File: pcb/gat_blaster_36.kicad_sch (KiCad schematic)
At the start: 25 parts, among them J1 Conn_01x05_Pin, J2 USB_C_Receptacle_USB2.0, SW1 SW_Push, SW2 SW_Push, U1 STM32F072CBTx, U2 TLV1117-33, Y1 8MHz

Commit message: Added USB 5V filter
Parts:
- added C12: 10n, symbol Device:C
- added C13: 100n, symbol Device:C
- added C14: 4.7u, symbol Device:C
- added C15, C16: 10p, symbol Device:C
- added FB2: 120, symbol Device:FerriteBead
- added R6, R7: 10R, symbol Device:R
- FB1: value 120 -> 120R
- R3: value 0 -> 0R
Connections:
- net GND: now also C12.2, C13.2, C14.2, C15.2, C16.2
- net SWCLK: now also D1.3 (IO2); no longer D1.6 (IO5)
- net SWDIO: now also D1.4 (IO3); no longer D1.5 (IO4)
- net USB_D+: now also D1.5 (IO4), R6.2; no longer D1.4 (IO3), J2.A6 (D+), J2.B6 (D+)
- net USB_D-: now also D1.6 (IO5), R7.2; no longer D1.3 (IO2), J2.A7 (D-), J2.B7 (D-)
- net VBUS: now also C12.1, FB2.1; no longer C10.1, U2.3 (VI)
- new net: C15.1, J2.A6 (D+), J2.B6 (D+), R6.1
- new net: C16.1, J2.A7 (D-), J2.B7 (D-), R7.1
- new net +5V: C10.1, C13.1, C14.1, FB2.2, U2.3 (VI)
- no-connect marks 1 -> 3
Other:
- moved on the sheet: C1, C10, C11, C2, C3, C4, C5, C6, C7, C8, C9, D1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

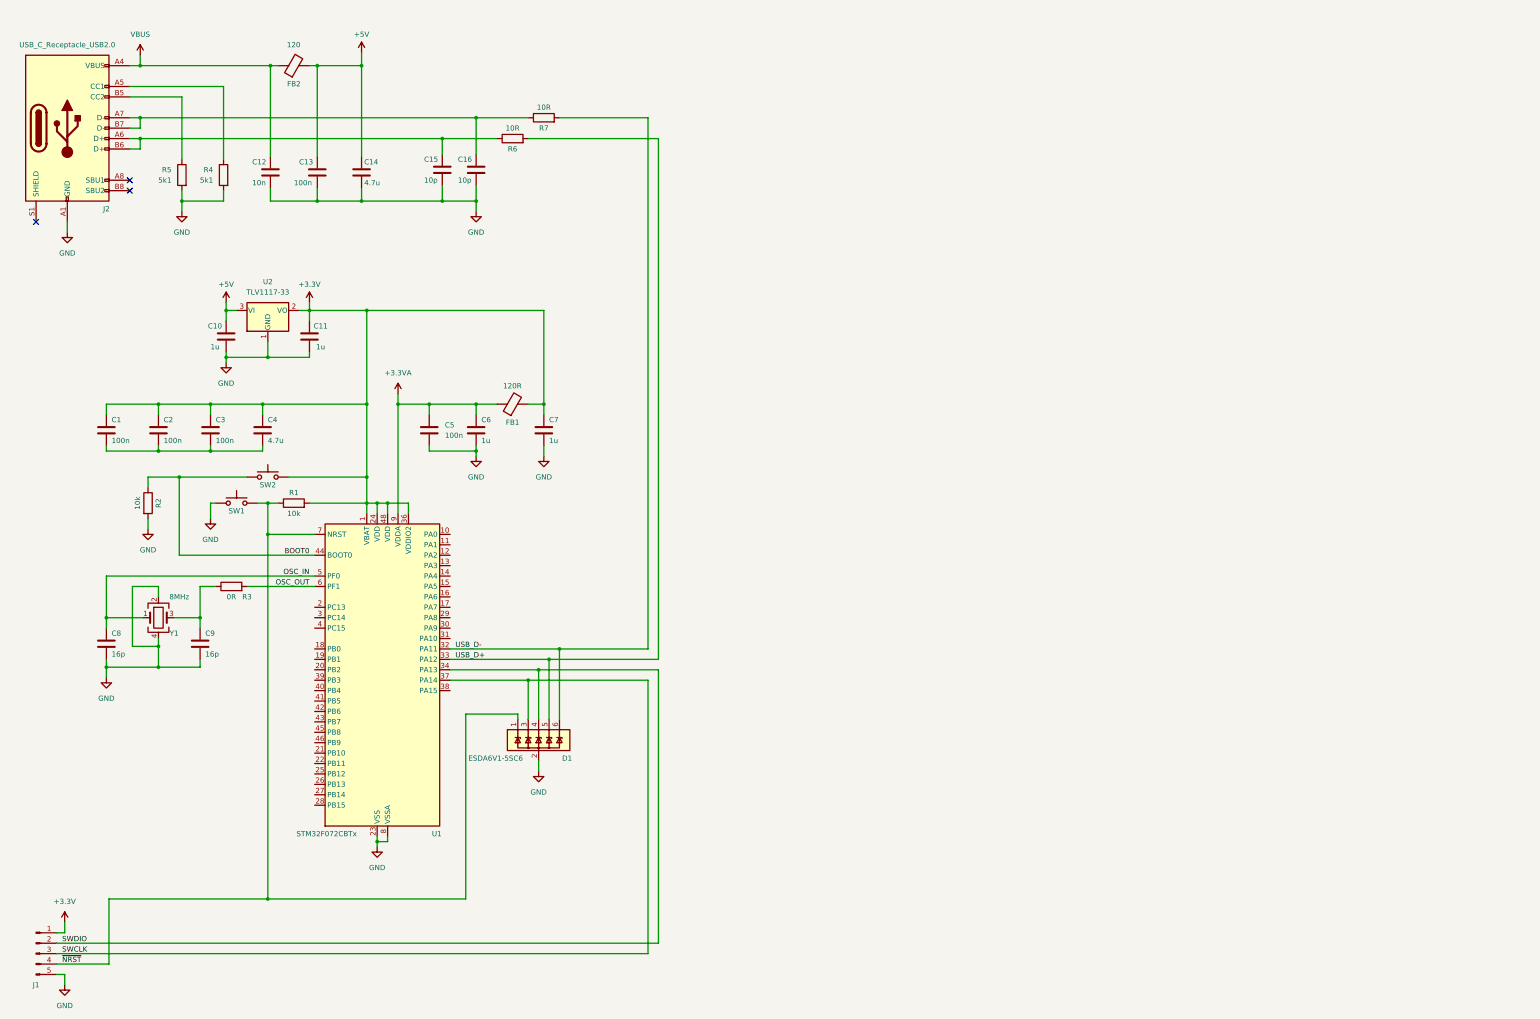
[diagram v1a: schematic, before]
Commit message: Added series resistors on data lines, changed left/right communication cable to HDMI connector, fully supported by single micro.
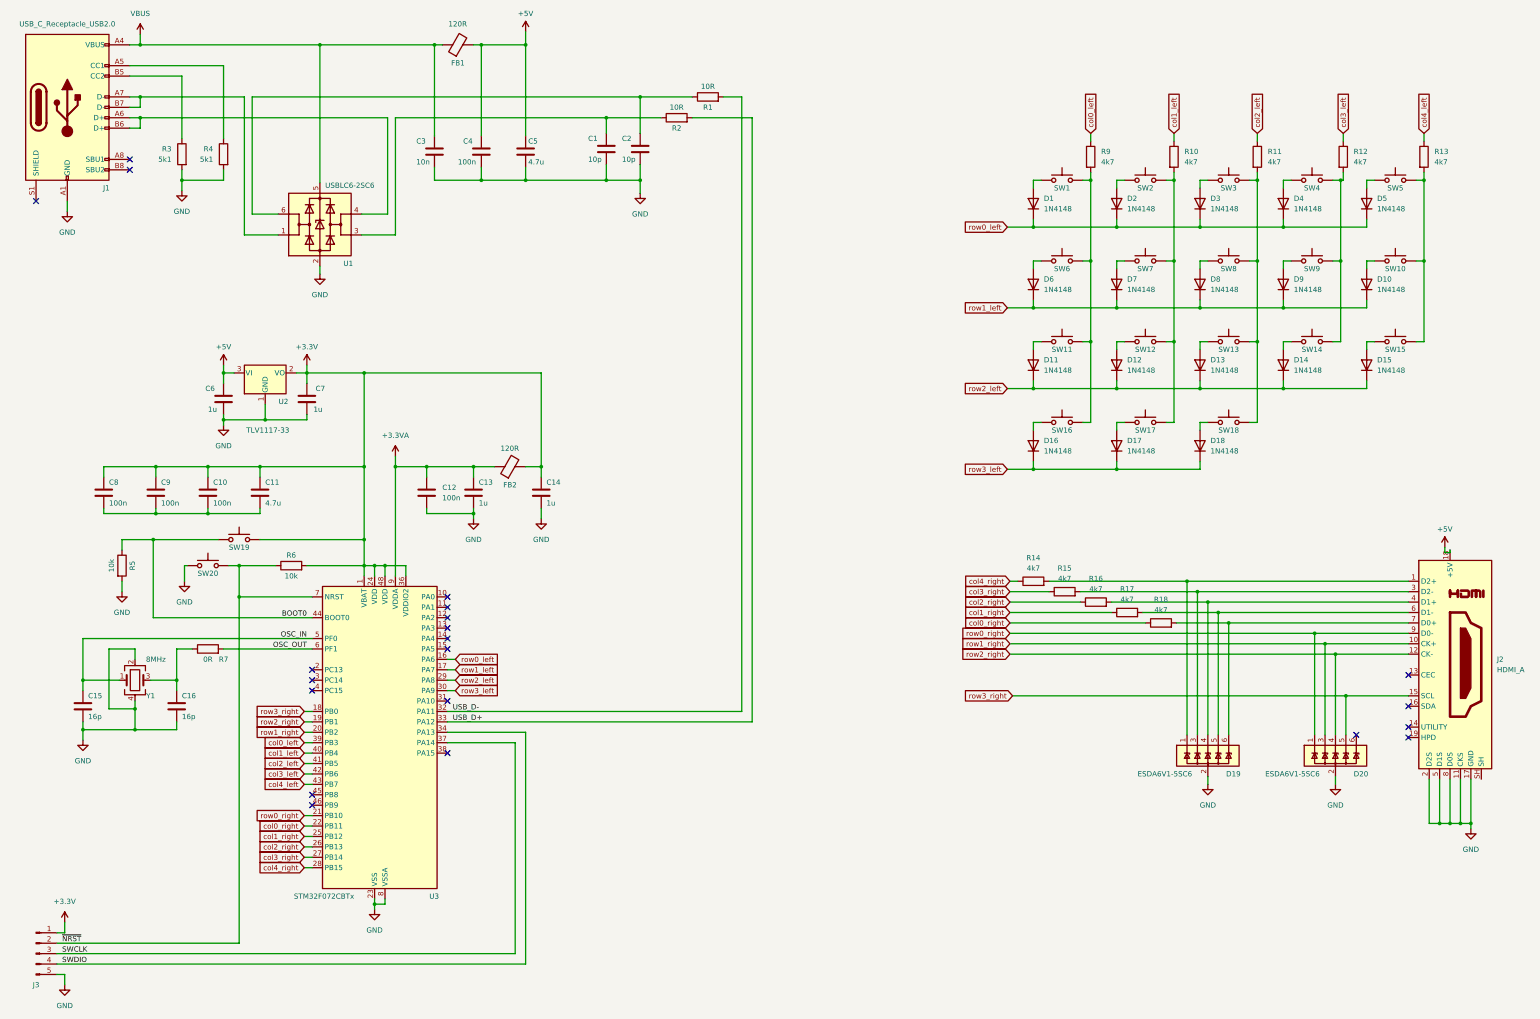
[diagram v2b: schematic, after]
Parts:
- removed D1: ESDA6V1-5SC6, Package_TO_SOT_SMD:SOT-23-6, symbol Power_Protection:ESDA6V1-5SC6
- added D1, D10, D11, D12, D13, D14, D15, D16, D17, D18, D2, D3, D4, D5, D6, D7, D8, D9: 1N4148, kbd:sod123_mmszxxxt1g, symbol Diode:1N4148
- added D19, D20: ESDA6V1-5SC6, kbd:sot23-6L_usblc6-2, symbol Power_Protection:ESDA6V1-5SC6
- added J2: HDMI_A, kbd:hdmi_cnc_tech_2000-1-1-20-00-bk, symbol Connector:HDMI_A
- added R10, R11, R12, R13, R14, R15, R16, R17, R18, R9: 4k7, kbd:0603, symbol Device:R
- added SW1, SW10, SW11, SW12, SW13, SW14, SW15, SW16, SW17, SW18, SW2, SW3, SW4, SW5, SW6, SW7, SW8, SW9: SW_Push, kbd:gateron_pro_5_reversible, symbol Switch:SW_Push
- added U1: USBLC6-2SC6, kbd:sot23-6L_usblc6-2, symbol Power_Protection:USBLC6-2SC6
- C1: renamed from C15; footprint (none) -> kbd:0603
- C10: renamed from C3; footprint (none) -> kbd:0603
- C11: renamed from C4; footprint (none) -> kbd:0603
- C12: renamed from C5; footprint (none) -> kbd:0603
- C13: renamed from C6; footprint (none) -> kbd:0603
- C14: renamed from C7; footprint (none) -> kbd:0603
- C15: renamed from C8; footprint (none) -> kbd:0603
- C16: renamed from C9; footprint (none) -> kbd:0603
- C2: renamed from C16; footprint (none) -> kbd:0603
- C3: renamed from C12; footprint (none) -> kbd:0603
- C4: renamed from C13; footprint (none) -> kbd:0603
- C5: renamed from C14; footprint (none) -> kbd:0603
- C6: renamed from C10; footprint (none) -> kbd:0603
- C7: renamed from C11; footprint (none) -> kbd:0603
- C8: renamed from C1; footprint (none) -> kbd:0603
- C9: renamed from C2; footprint (none) -> kbd:0603
- FB1: renamed from FB2; value 120 -> 120R; footprint (none) -> kbd:0603
- FB2: renamed from FB1; footprint (none) -> kbd:0603
- J1: renamed from J2; footprint (none) -> kbd:usb-c_usb4085
- J3: renamed from J1; footprint (none) -> kbd:SIP-5
- R1: renamed from R7; footprint (none) -> kbd:0603
- R2: renamed from R6; footprint (none) -> kbd:0603
- R3: renamed from R5; footprint (none) -> kbd:0603
- R4: footprint (none) -> kbd:0603
- R5: renamed from R2; footprint (none) -> kbd:0603
- R6: renamed from R1; footprint (none) -> kbd:0603
- R7: renamed from R3; footprint (none) -> kbd:0603
- SW19: renamed from SW2; footprint (none) -> kbd:sw_pts647
- SW20: renamed from SW1; footprint (none) -> kbd:sw_pts647
- U2: footprint (none) -> kbd:sot223_tl1117
- U3: renamed from U1; footprint Package_QFP:LQFP-48_7x7mm_P0.5mm -> kbd:QFP-48_7x7_Pitch0.5mm
- Y1: footprint (none) -> kbd:osc_ecx-32
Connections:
- net +5V: now also J2.18 (+5V)
- net GND: now also D19.2 (GND), D20.2 (GND), J2.11 (CKS), J2.17 (GND), J2.2 (D2S), J2.5 (D1S), J2.8 (D0S), U1.2 (GND)
- net SWDIO: now also J3.4 (Pin_4); no longer J3.2 (Pin_2)
- net VBUS: now also U1.5 (VBUS)
- net ~{NRST}: now also J3.2 (Pin_2); no longer J3.4 (Pin_4)
- net at C1.1, R2.1: now also U1.3 (I/O2); no longer J1.A6 (D+), J1.B6 (D+)
- net at C2.1, R1.1: now also U1.6 (I/O1); no longer J1.A7 (D-), J1.B7 (D-)
- net row0_left: now reaches U3.16 (PA6)
- net row0_left: now also D1.1 (K), D2.1 (K), D3.1 (K), D4.1 (K), D5.1 (K)
- net row1_left: now reaches U3.17 (PA7)
- net row1_left: now also D10.1 (K), D6.1 (K), D7.1 (K), D8.1 (K), D9.1 (K)
- net row3_right: now reaches U3.18 (PB0)
- net row3_right: now also D20.5 (IO4), J2.15 (SCL)
- net row2_right: now reaches U3.19 (PB1)
- net row2_right: now also D20.4 (IO3), J2.12 (CK-)
- net row1_right: now reaches U3.20 (PB2)
- net row1_right: now also D20.3 (IO2), J2.10 (CK+)
- net row0_right: now reaches U3.21 (PB10)
- net row0_right: now also D20.1 (IO1), J2.9 (D0-)
- net col0_right: now reaches U3.22 (PB11)
- net col0_right: now also R18.1
- net col1_right: now reaches U3.25 (PB12)
- net col1_right: now also R17.1
- net col2_right: now reaches U3.26 (PB13)
- net col2_right: now also R16.1
- net col3_right: now reaches U3.27 (PB14)
- net col3_right: now also R15.1
- net col4_right: now reaches U3.28 (PB15)
- net col4_right: now also R14.1
- net row2_left: now reaches U3.29 (PA8)
- net row2_left: now also D11.1 (K), D12.1 (K), D13.1 (K), D14.1 (K), D15.1 (K)
- net row3_left: now reaches U3.30 (PA9)
- net row3_left: now also D16.1 (K), D17.1 (K), D18.1 (K)
- net col0_left: now reaches U3.39 (PB3)
- net col0_left: now also R9.1
- net col1_left: now reaches U3.40 (PB4)
- net col1_left: now also R10.1
- net col2_left: now reaches U3.41 (PB5)
- net col2_left: now also R11.1
- net col3_left: now reaches U3.42 (PB6)
- net col3_left: now also R12.1
- net col4_left: now reaches U3.43 (PB7)
- net col4_left: now also R13.1
- new net: D9.2 (A), SW9.1
- new net: R12.2, SW14.2, SW4.2, SW9.2
- new net: D1.2 (A), SW1.1
- new net: R9.2, SW1.2, SW11.2, SW16.2, SW6.2
- new net: D11.2 (A), SW11.1
- new net: D19.4 (IO3), J2.4 (D1+), R16.2
- new net: R11.2, SW13.2, SW18.2, SW3.2, SW8.2
- new net: D15.2 (A), SW15.1
- new net: R13.2, SW10.2, SW15.2, SW5.2
- new net: D16.2 (A), SW16.1
- new net: D10.2 (A), SW10.1
- new net: D19.6 (IO5), J2.7 (D0+), R18.2
- new net: D13.2 (A), SW13.1
- new net: D6.2 (A), SW6.1
- new net: D8.2 (A), SW8.1
- new net: D12.2 (A), SW12.1
- new net: R10.2, SW12.2, SW17.2, SW2.2, SW7.2
- new net: D2.2 (A), SW2.1
- new net: D14.2 (A), SW14.1
- new net: D5.2 (A), SW5.1
- new net: D19.5 (IO4), J2.6 (D1-), R17.2
- new net: D17.2 (A), SW17.1
- new net: D3.2 (A), SW3.1
- new net: J1.A6 (D+), J1.B6 (D+), U1.4 (I/O2)
- new net: J1.A7 (D-), J1.B7 (D-), U1.1 (I/O1)
- new net: D4.2 (A), SW4.1
- new net: D19.1 (IO1), J2.1 (D2+), R14.2
- new net: D19.3 (IO2), J2.3 (D2-), R15.2
- new net: D7.2 (A), SW7.1
- new net: D18.2 (A), SW18.1
- no-connect marks 3 -> 21
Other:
- moved on the sheet: C1, C10, C11, C12, C13, C14, C15, C16, C2, C3, C4, C5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
